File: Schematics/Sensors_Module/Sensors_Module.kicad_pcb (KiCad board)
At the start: 2 copper layers, 69.5 x 60 mm, 1 part, among them J6 Stack Male Edge Connector

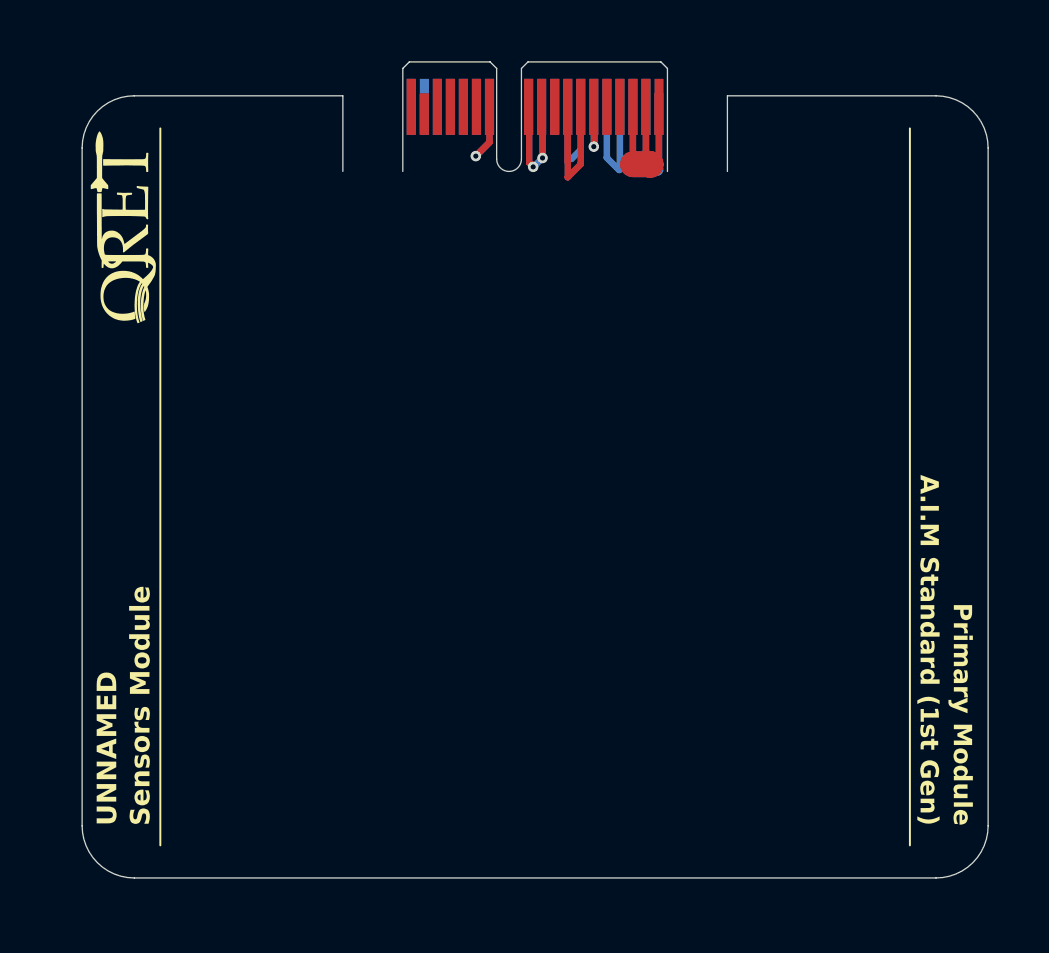
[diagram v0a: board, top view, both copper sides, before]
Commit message: Completed PCB layout
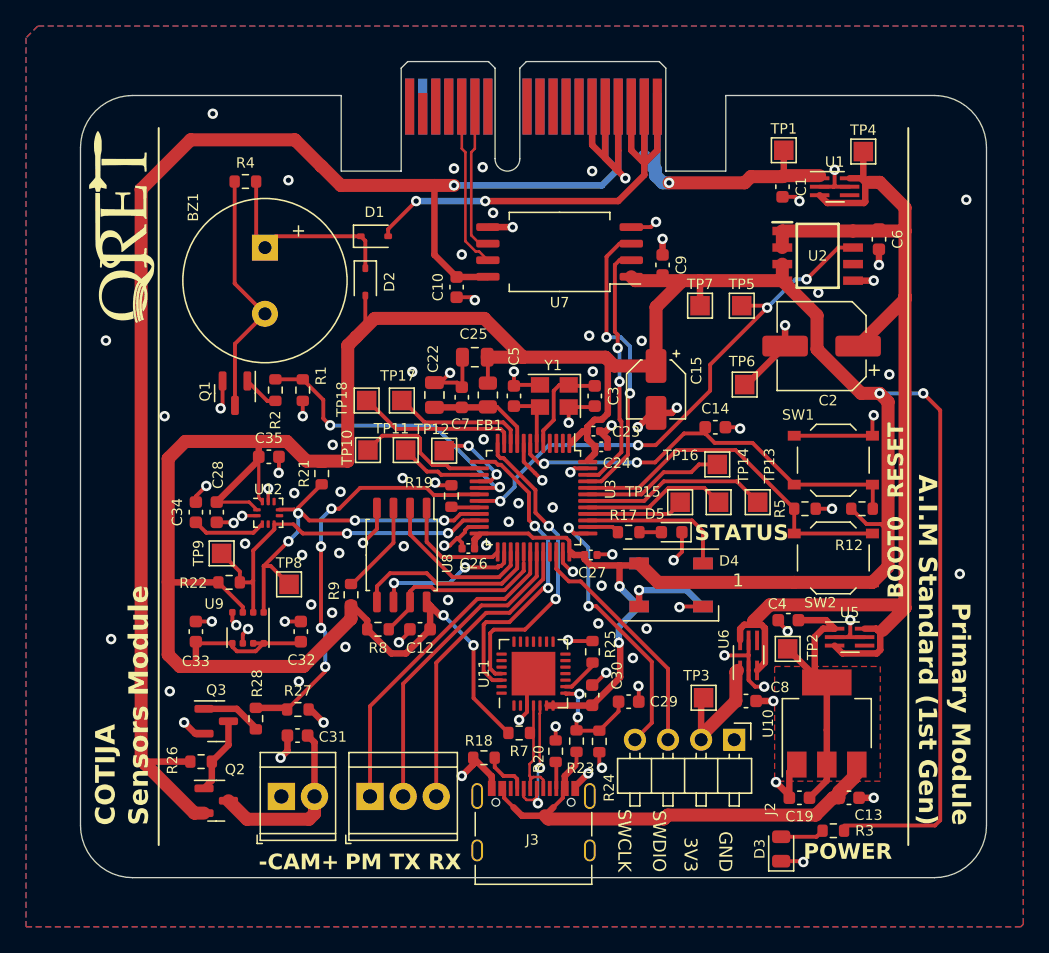
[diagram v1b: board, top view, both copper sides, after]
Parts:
- added BZ1: PKM13EPYH4000, footprints:Buzzer_12.6x9.5RM5.0, F.Cu at (101.1, 58.5)
- added C1: 1uF, Capacitor_SMD:C_0603_1608Metric, F.Cu at (140.8, 55.1)
- added C10: 0.1u, Capacitor_SMD:C_0603_1608Metric, F.Cu at (115.8, 62.8)
- added C12: 100nF, Capacitor_SMD:C_0603_1608Metric, F.Cu at (113.0, 89.0)
- added C13: 10uF, Capacitor_SMD:C_0603_1608Metric, F.Cu at (145.9, 102.0)
- added C14: 100nF, Capacitor_SMD:C_0603_1608Metric, F.Cu at (135.7, 73.5)
- added C15: 10uF, Capacitor_SMD:CP_Elec_4x5.4, F.Cu at (131.1, 70.7)
- added C19: 10uF, Capacitor_SMD:C_0603_1608Metric, F.Cu at (142.1, 102.0)
- added C2: 100uF, Capacitor_SMD:CP_Elec_6.3x5.9, F.Cu at (143.8, 67.3)
- added C22: 1uF, Capacitor_SMD:C_0805_2012Metric, F.Cu at (114.1, 71.1)
- added C23: 100n, Capacitor_SMD:C_0402_1005Metric, F.Cu at (126.3, 73.8)
- added C24: 100n, Capacitor_SMD:C_0402_1005Metric, F.Cu at (126.9, 75.0)
- added C25: 1uF, Capacitor_SMD:C_0805_2012Metric, F.Cu at (117.2, 68.2)
- added C26: 100n, Capacitor_SMD:C_0402_1005Metric, F.Cu at (116.7, 82.8)
- added C27: 100n, Capacitor_SMD:C_0402_1005Metric, F.Cu at (126.1, 83.3)
- added C28: 1uF, Capacitor_SMD:C_0603_1608Metric, F.Cu at (97.4, 80.1)
- added C29: 1uF, Capacitor_SMD:C_0603_1608Metric, F.Cu at (129.0, 94.6)
- added C3: 10p, Capacitor_SMD:C_0603_1608Metric, F.Cu at (126.4, 71.2)
- added C30: 10uF, Capacitor_SMD:C_0603_1608Metric, F.Cu at (126.2, 94.1)
- added C31: 10uF, Capacitor_SMD:C_0603_1608Metric, F.Cu at (103.6, 97.2)
- added C32: 100nF, Capacitor_SMD:C_0603_1608Metric, F.Cu at (103.8, 89.2)
- added C33: 100nF, Capacitor_SMD:C_0603_1608Metric, F.Cu at (95.8, 89.2)
- added C34: 1uF, Capacitor_SMD:C_0603_1608Metric, F.Cu at (95.8, 80.1)
- added C35: 1uF, Capacitor_SMD:C_0603_1608Metric, F.Cu at (101.4, 75.8)
- added C4: 1uF, Capacitor_SMD:C_0603_1608Metric, F.Cu at (141.2, 88.3)
- added C5: 10p, Capacitor_SMD:C_0603_1608Metric, F.Cu at (120.2, 71.2)
- added C6: 0.1uF, Capacitor_SMD:C_0603_1608Metric, F.Cu at (148.2, 59.1)
- added C7: 10n, Capacitor_SMD:C_0603_1608Metric, F.Cu at (116.2, 71.2)
- added C8: 1uF, Capacitor_SMD:C_0603_1608Metric, F.Cu at (138.0, 94.5)
- added C9: 0.1u, Capacitor_SMD:C_0603_1608Metric, F.Cu at (131.6, 61.1)
- added D1: 1N5819WS, Diode_SMD:D_SOD-323, F.Cu at (109.5, 58.9)
- added D2: 1N5819WS, Diode_SMD:D_SOD-323, F.Cu at (108.8, 62.4)
- added D3: PWR_LED (GRN), LED_SMD:LED_0805_2012Metric, F.Cu at (140.7, 105.9)
- added D4: WS2812B, LED_SMD:LED_WS2812B_PLCC4_5.0x5.0mm_P3.2mm, F.Cu at (132.2, 85.7)
- added D5: DB_LED (YLW), LED_SMD:LED_0603_1608Metric, F.Cu at (132.3, 81.6)
- added D6: WS2812B, LED_SMD:LED_WS2812B_PLCC4_5.0x5.0mm_P3.2mm, B.Cu at (132.2, 85.7)
- added FB1: 100R, Resistor_SMD:R_0805_2012Metric, F.Cu at (118.2, 71.1)
- added J1: Stack Male Edge Connector, Connector_PCBEdge:BUS_PCIexpress_x1, F.Cu at (131.2, 49.0)
- added J2: SWD_01x04_Pin, SWD_Header:SWD_PinHeader_1x04_P2.54mm_Horizontal, F.Cu at (137.1, 97.5)
- added J3: USB_C_Female_USB2_Small, footprints:USB_C_DB-108PWB, F.Cu at (121.7, 103.8)
- added J7: CAM_DAT, TerminalBlock_TE-Connectivity:TerminalBlock_TE_282834-3_1x03_P2.54mm_Horizontal, F.Cu at (109.2, 101.9)
- added Q1: AO3400A, Package_TO_SOT_SMD:SOT-23, F.Cu at (98.8, 70.9)
- added Q2: AO3401A, Package_TO_SOT_SMD:SOT-23, F.Cu at (97.4, 102.2)
- added Q3: AO3400A, Package_TO_SOT_SMD:SOT-23, F.Cu at (97.4, 96.1)
- added R1: 10k, Resistor_SMD:R_0603_1608Metric, F.Cu at (104.0, 70.7)
- added R12: 10k, Resistor_SMD:R_0603_1608Metric, F.Cu at (146.9, 79.8)
- added R17: 680R, Resistor_SMD:R_0603_1608Metric, F.Cu at (129.0, 81.6)
- added R18: 5.1k, Resistor_SMD:R_0603_1608Metric, F.Cu at (117.9, 98.9)
- added R19: 100k, Resistor_SMD:R_0603_1608Metric, F.Cu at (115.4, 78.8)
- added R2: 510R, Resistor_SMD:R_0603_1608Metric, F.Cu at (101.9, 70.7)
- added R20: 5.1k, Resistor_SMD:R_0603_1608Metric, F.Cu at (123.4, 98.4)
- added R21: 4.7k, Resistor_SMD:R_0603_1608Metric, F.Cu at (105.5, 77.1)
- added R22: 4.7k, Resistor_SMD:R_0603_1608Metric, F.Cu at (98.3, 85.5)
- added R23: 22k, Resistor_SMD:R_0603_1608Metric, F.Cu at (125.0, 97.6)
- added R24: 47k, Resistor_SMD:R_0603_1608Metric, F.Cu at (126.8, 97.7)
- added R25: 1k, Resistor_SMD:R_0603_1608Metric, F.Cu at (126.2, 90.8)
- added R26: 100k, Resistor_SMD:R_0603_1608Metric, F.Cu at (96.2, 99.2)
- added R27: 100k, Resistor_SMD:R_0603_1608Metric, F.Cu at (103.6, 95.2)
- added R28: 510, Resistor_SMD:R_0603_1608Metric, F.Cu at (100.4, 95.9)
- added R3: 3.3k, Resistor_SMD:R_0603_1608Metric, F.Cu at (144.7, 104.5)
- added R4: 1k, Resistor_SMD:R_0603_1608Metric, F.Cu at (99.6, 54.7)
- added R5: 100k, Resistor_SMD:R_0603_1608Metric, F.Cu at (142.5, 79.8)
- added R7: 1.5k, Resistor_SMD:R_0603_1608Metric, F.Cu at (120.6, 97.0)
- added R8: 10k, Resistor_SMD:R_0603_1608Metric, F.Cu at (109.8, 89.0)
- added R9: 10k, Resistor_SMD:R_0603_1608Metric, F.Cu at (107.7, 86.4)
- added SW1: SW_STM_RESET, Button_Switch_SMD:SW_Push_1P1T_XKB_TS-1187A, F.Cu at (144.7, 76.1)
- added SW2: SW_STM_BOOT_MODE, Button_Switch_SMD:SW_Push_1P1T_XKB_TS-1187A, F.Cu at (144.7, 83.6)
- added TP1: TP_VSTACK, TestPoint:TestPoint_Pad_1.5x1.5mm, F.Cu at (140.9, 52.3)
- added TP10: PA4, TestPoint:TestPoint_Pad_1.5x1.5mm, F.Cu at (109.0, 75.3)
- added TP11: PA5, TestPoint:TestPoint_Pad_1.5x1.5mm, F.Cu at (111.9, 75.3)
- added TP12: PA6, TestPoint:TestPoint_Pad_1.5x1.5mm, F.Cu at (114.8, 75.3)
- added TP13: PB6, TestPoint:TestPoint_Pad_1.5x1.5mm, F.Cu at (138.9, 79.3)
- added TP14: PB5, TestPoint:TestPoint_Pad_1.5x1.5mm, F.Cu at (135.9, 79.3)
- added TP15: PB4, TestPoint:TestPoint_Pad_1.5x1.5mm, F.Cu at (132.9, 79.3)
- added TP16: PB7, TestPoint:TestPoint_Pad_1.5x1.5mm, F.Cu at (135.8, 76.4)
- added TP17: PA0, TestPoint:TestPoint_Pad_1.5x1.5mm, F.Cu at (111.6, 71.5)
- added TP18: PA1, TestPoint:TestPoint_Pad_1.5x1.5mm, F.Cu at (108.9, 71.5)
- added TP2: TP_VUSB, TestPoint:TestPoint_Pad_1.5x1.5mm, F.Cu at (141.2, 90.5)
- added TP3: TP_VSWD, TestPoint:TestPoint_Pad_1.5x1.5mm, F.Cu at (134.8, 94.3)
- added TP4: TP_MUX, TestPoint:TestPoint_Pad_1.5x1.5mm, F.Cu at (147.0, 52.4)
- added TP5: TP_ISENSE, TestPoint:TestPoint_Pad_1.5x1.5mm, F.Cu at (137.7, 64.2)
- added TP6: TP_GND, TestPoint:TestPoint_Pad_1.5x1.5mm, F.Cu at (137.9, 70.3)
- added TP7: TP_3V3, TestPoint:TestPoint_Pad_1.5x1.5mm, F.Cu at (134.5, 64.2)
- added TP8: TP_SCL, TestPoint:TestPoint_Pad_1.5x1.5mm, F.Cu at (103.0, 85.6)
- added TP9: TP_SDA, TestPoint:TestPoint_Pad_1.5x1.5mm, F.Cu at (97.8, 83.2)
- added U1: LM66100DCKR, LMR66100:SC-70-6_Handsoldering, F.Cu at (144.8, 55.1)
- added U10: AMS1117-3.3, Package_TO_SOT_SMD:SOT-223-3_TabPin2, F.Cu at (144.2, 96.3)
- added U11: CP2102N-Axx-xQFN28, Package_DFN_QFN:QFN-28-1EP_5x5mm_P0.5mm_EP3.35x3.35mm, F.Cu at (121.7, 92.5)
- added U12: BM1422AGMV, Package_LGA:Rohm_MLGA010V020A_LGA-10_2x2mm_P0.45mm_LayoutBorder_3x2y, F.Cu at (101.3, 80.1)
- added U2: ACS70331EOLC, footprints:SOIC127P600X175-8N, F.Cu at (143.5, 60.4)
- added U3: STM32F103CBT6, Package_QFP:LQFP-48_7x7mm_P0.5mm, F.Cu at (121.7, 79.0)
- added U5: LM66100DCKR, LMR66100:SC-70-6_Handsoldering, F.Cu at (145.9, 89.7)
- added U6: LM66100DCKR, LMR66100:SC-70-6_Handsoldering, F.Cu at (138.2, 91.0)
- added U7: ISO1042BDWVR, ISO1042:SOIC-8 ISO1042BDWV, F.Cu at (123.7, 60.1)
- added U8: W25Q128JVS, Package_SO:SOIC-8_5.23x5.23mm_P1.27mm, F.Cu at (111.6, 83.3)
- added U9: BME680, Package_LGA:Bosch_LGA-8_3x3mm_P0.8mm_ClockwisePinNumbering, F.Cu at (99.8, 88.9)
- added Y1: X322516MMB4SI, Crystal:Crystal_SMD_3225-4Pin_3.2x2.5mm, F.Cu at (123.3, 71.2)
- J6: value Stack Male Edge Connector -> CAM_PWR; footprint Connector_PCBEdge:BUS_PCIexpress_x1 -> TerminalBlock_TE-Connectivity:TerminalBlock_TE_282834-2_1x02_P2.54mm_Horizontal
- moved J6 60.3 mm to (102.4, 101.9), turned to 0 degrees
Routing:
- net +3.3V: track 0.00 -> 304.0 mm, vias 0 -> 6
- net GND: track 0.00 -> 145.2 mm, vias 0 -> 100
- net +5V: track 0.00 -> 114.1 mm, vias 0 -> 1
- net V_MUX: track 0.00 -> 87.1 mm
- net (no net): track 78.1 -> 0.00 mm, vias 4 -> 0
- net CURR_SENSE: track 0.00 -> 40.3 mm, vias 0 -> 4
- net 5V_RAW: track 0.00 -> 39.9 mm
- net +BATT: track 0.00 -> 36.7 mm, vias 0 -> 2
- net STM_RESET: track 0.00 -> 32.3 mm, vias 0 -> 2
- net CAM_PWR: track 0.00 -> 31.8 mm, vias 0 -> 4
- net SCL: track 0.00 -> 30.1 mm, vias 0 -> 4
- net SDA: track 0.00 -> 27.8 mm, vias 0 -> 2
- net BOOT0: track 0.00 -> 26.8 mm
- net CAM_TX: track 0.00 -> 25.1 mm
- net V_PSU: track 0.00 -> 25.0 mm, vias 0 -> 1
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- added copper zone on B.Cu, net GND
- added copper zone on F.Cu, net GND
- added copper zone on F.Cu, net V_REGUSB
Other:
- outline, holes or cut-outs redrawn
- board text added: "-CAM+"
- board text added: "BOOT0"
- board text added: "COTIJA"
- board text added: "Cotija Rev 1.0 QRET May 2024 Ethan Toste Kennan Bays"
- board text added: "JLCJLCJLCJLC"
- board text added: "PM TX RX"
- board text added: "POWER"
- board text added: "RESET"
- board text added: "STATUS"
- board text removed: "UNNAMED"

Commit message: Final tweaks
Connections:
- net D+ renamed CAN_H
- net D- renamed CAN_L
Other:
- board text added: "."
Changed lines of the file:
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@@
       (plot_on_all_layers_selection 0x0000000_00000000)
       (disableapertmacros false)
-      (usegerberextensions false)
-      (usegerberattributes true)
-      (usegerberadvancedattributes true)
-      (creategerberjobfile true)
+      (usegerberextensions true)
+      (usegerberattributes false)
+      (usegerberadvancedattributes false)
+      (creategerberjobfile false)
       (dashed_line_dash_ratio 12.000000)
       (dashed_line_gap_ratio 3.000000)
@@
       (psa4output false)
       (plotreference true)
-      (plotvalue true)
+      (plotvalue false)
       (plotinvisibletext false)
       (sketchpadsonfab false)
-      (subtractmaskfromsilk false)
+      (subtractmaskfromsilk true)
       (outputformat 1)
       (mirror false)
-      (drillshape 1)
+      (drillshape 0)
       (scaleselection 1)
-      (outputdirectory "")
+      (outputdirectory "gerbers/")
     )
   )
@@
   (net 110 "unconnected-(U12-TEST2-Pad6)")
   (net 111 "unconnected-(U12-DRDY-Pad8)")
-  (net 112 "D+")
-  (net 113 "D-")
+  (net 112 "CAN_L")
+  (net 113 "CAN_H")
   (footprint "Resistor_SMD:R_0603_1608Metric" (layer "F.Cu")
     (at 104 70.7 90)
@@
       (net 4 "GND") (pinfunction "GND2") (pintype "power_in"))
     (pad "6" smd roundrect (at 5.5 0.635 180) (size 1.8 0.6) (layers "F.Cu" "F.Paste" "F.Mask") (roundrect_rratio 0.25)
-      (net 113 "D-") (pinfunction "CANL") (pintype "bidirectional"))
+      (net 112 "CAN_L") (pinfunction "CANL") (pintype "bidirectional"))
     (pad "7" smd roundrect (at 5.5 -0.635 180) (size 1.8 0.6) (layers "F.Cu" "F.Paste" "F.Mask") (roundrect_rratio 0.25)
-      (net 112 "D+") (pinfunction "CANH") (pintype "bidirectional"))
+      (net 113 "CAN_H") (pinfunction "CANH") (pintype "bidirectional"))
     (pad "8" smd roundrect (at 5.5 -1.905 180) (size 1.8 0.6) (layers "F.Cu" "F.Paste" "F.Mask") (roundrect_rratio 0.25)
       (net 12 "+5V") (pinfunction "VCC2") (pintype "power_in"))
@@
       (net 25 "unconnected-(J1-GND_B-PadA12)") (pinfunction "GND_B") (pintype "passive+no_connect"))
     (pad "B13" connect rect (at 14 0 180) (size 0.7 4.3) (layers "F.Cu" "F.Mask")
-      (net 113 "D-") (pinfunction "CAN_L") (pintype "bidirectional"))
+      (net 112 "CAN_L") (pinfunction "CAN_L") (pintype "bidirectional"))
     (pad "B14" connect rect (at 15 0 180) (size 0.7 4.3) (layers "F.Cu" "F.Mask")
-      (net 112 "D+") (pinfunction "CAN_H") (pintype "bidirectional"))
+      (net 113 "CAN_H") (pinfunction "CAN_H") (pintype "bidirectional"))
     (pad "B15" connect rect (at 16 0 180) (size 0.7 4.3) (layers "F.Cu" "F.Mask")
       (net 35 "unconnected-(J1-Reserved-PadB15)") (pinfunction "Reserved") (pintype "no_connect"))
@@
     (fp_line (start 1 0.625) (end -1 0.625)
       (stroke (width 0.1) (type solid)) (layer "F.Fab"))
-    (pad "1" smd roundrect (at -0.9125 0 90) (size 1.025 1.4) (layers "F.Cu" "F.Paste" "F.Mask") (roundrect_rratio 0.243902)
+    (pad "1" smd roundrect (at -0.9125 0 90) (size 1.025 1.4) (layers "F.Cu" "F.Paste" "F.Mask") (roundrect_rratio 0.243902439)
       (net 9 "+3.3VA") (pintype "passive"))
-    (pad "2" smd roundrect (at 0.9125 0 90) (size 1.025 1.4) (layers "F.Cu" "F.Paste" "F.Mask") (roundrect_rratio 0.243902)
+    (pad "2" smd roundrect (at 0.9125 0 90) (size 1.025 1.4) (layers "F.Cu" "F.Paste" "F.Mask") (roundrect_rratio 0.243902439)
       (net 11 "+3.3V") (pintype "passive"))
     (model "${KICAD6_3DMODEL_DIR}/Resistor_SMD.3dshapes/R_0805_2012Metric.wrl"
@@
     (effects (font (size 1.2 1.2) (thickness 0.2) bold) (justify left bottom))
   )
+  (gr_text "." (at 98.2 87) (layer "F.SilkS")
+    (effects (font (size 1.2 1.2) (thickness 0.24) bold) (justify left bottom))
+  )
   (gr_text "Primary Module" (at 153.65 104.099998 270) (layer "F.SilkS")
     (effects (font (size 1.4 1.4) (thickness 0.25) bold) (justify right bottom))
@@
   (segment (start 128.3 70.05) (end 128.3 67.610663) (width 0.3) (layer "B.Cu") (net 87))
   (segment (start 128.3 67.610663) (end 128.15962 67.470283) (width 0.3) (layer "B.Cu") (net 87))
-  (segment (start 117.263604 60.065) (end 116.475 59.276396) (width 0.2) (layer "F.Cu") (net 112))
-  (segment (start 117.53 60.065) (end 117.263604 60.065) (width 0.2) (layer "F.Cu") (net 112))
-  (segment (start 116.475 59.276396) (end 116.475 52.450001) (width 0.2) (layer "F.Cu") (net 112))
-  (segment (start 116.2 52.175001) (end 116.2 48.95) (width 0.2) (layer "F.Cu") (net 112))
-  (segment (start 118.2 60.735) (end 117.53 60.065) (width 0.2) (layer "F.Cu") (net 112))
-  (segment (start 116.475 52.450001) (end 116.2 52.175001) (width 0.2) (layer "F.Cu") (net 112))
-  (segment (start 118.2 59.465) (end 117.566397 59.465) (width 0.2) (layer "F.Cu") (net 113))
-  (segment (start 116.925 58.823603) (end 116.925 52.450001) (width 0.2) (layer "F.Cu") (net 113))
-  (segment (start 117.2 52.175001) (end 117.2 48.95) (width 0.2) (layer "F.Cu") (net 113))
-  (segment (start 117.566397 59.465) (end 116.925 58.823603) (width 0.2) (layer "F.Cu") (net 113))
-  (segment (start 116.925 52.450001) (end 117.2 52.175001) (width 0.2) (layer "F.Cu") (net 113))
+  (segment (start 118.2 59.465) (end 117.566397 59.465) (width 0.2) (layer "F.Cu") (net 112))
+  (segment (start 116.925 58.823603) (end 116.925 52.450001) (width 0.2) (layer "F.Cu") (net 112))
+  (segment (start 117.2 52.175001) (end 117.2 48.95) (width 0.2) (layer "F.Cu") (net 112))
+  (segment (start 117.566397 59.465) (end 116.925 58.823603) (width 0.2) (layer "F.Cu") (net 112))
+  (segment (start 116.925 52.450001) (end 117.2 52.175001) (width 0.2) (layer "F.Cu") (net 112))
+  (segment (start 117.263604 60.065) (end 116.475 59.276396) (width 0.2) (layer "F.Cu") (net 113))
+  (segment (start 117.53 60.065) (end 117.263604 60.065) (width 0.2) (layer "F.Cu") (net 113))
+  (segment (start 116.475 59.276396) (end 116.475 52.450001) (width 0.2) (layer "F.Cu") (net 113))
+  (segment (start 116.2 52.175001) (end 116.2 48.95) (width 0.2) (layer "F.Cu") (net 113))
+  (segment (start 118.2 60.735) (end 117.53 60.065) (width 0.2) (layer "F.Cu") (net 113))
+  (segment (start 116.475 52.450001) (end 116.2 52.175001) (width 0.2) (layer "F.Cu") (net 113))
   (zone locked (net 7) (net_name "V_REGUSB") (layer "F.Cu") (name "Keepout") (hatch edge 0.5)
     (priority 1)

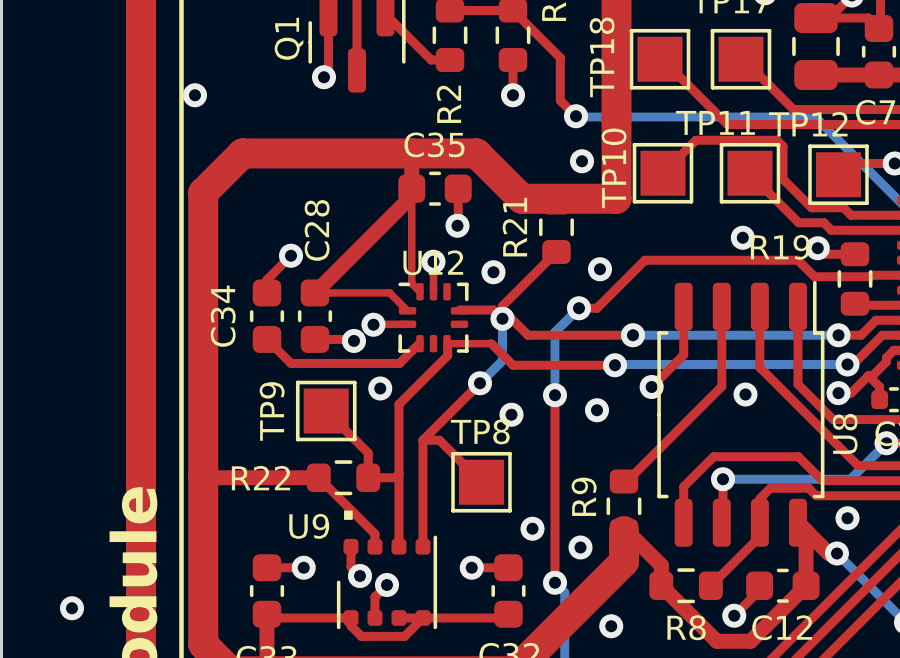
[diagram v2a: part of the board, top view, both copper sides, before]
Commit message: Fixed incorrect pinout for BM1422AGMV (Rev 1.0A)
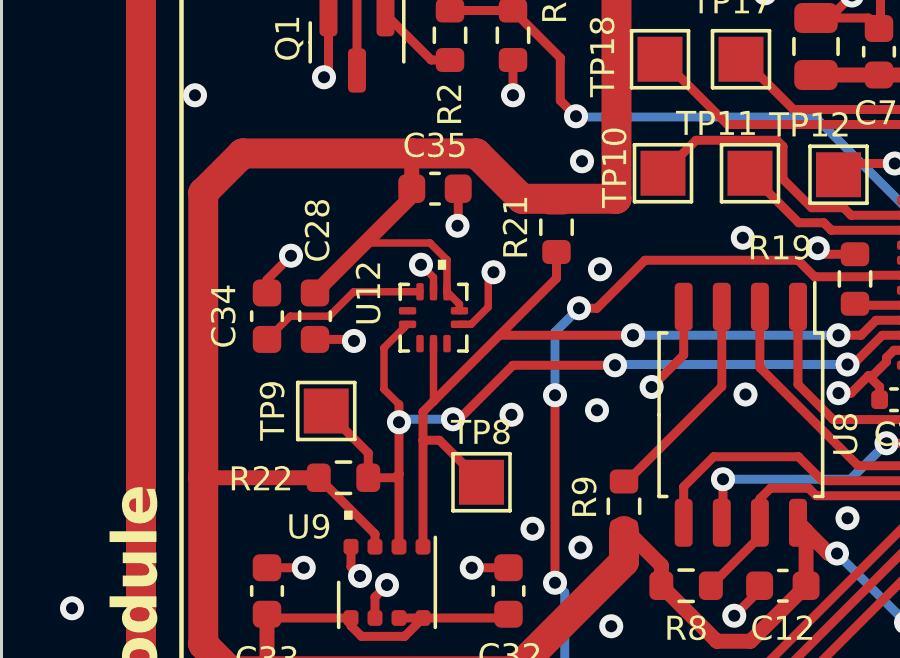
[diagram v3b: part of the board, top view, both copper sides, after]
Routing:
- net SDA: track 27.8 -> 30.4 mm, vias 2 -> 4
- net GND: track 145.2 -> 146.6 mm, vias 100 -> 98
- net SCL: track 30.1 -> 30.3 mm, vias 4 -> 2
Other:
- board text added: "Cotija Rev 1.0A QRET May 2024 Ethan Toste Kennan Bays"
- board text removed: "Cotija Rev 1.0 QRET May 2024 Ethan Toste Kennan Bays"

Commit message: Version bump to V2.0
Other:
- board text added: "COTIJA V2.0"
- board text added: "Cotija Rev 2.0 QRET Mar 2025 Ethan Toste Kennan Bays"
- board text removed: "COTIJA"
- board text removed: "Cotija Rev 1.0A QRET May 2024 Ethan Toste Kennan Bays"
- board text removed: "JLCJLCJLCJLC"
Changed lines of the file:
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@@
   (gr_line (start 106.95 53.9) (end 111.55 53.9)
     (stroke (width 0.1) (type default)) (layer "Edge.Cuts"))
-  (gr_text "Cotija Rev 1.0A\nQRET May 2024\n\nEthan Toste\nKennan Bays" (at 121.699999 57.3) (layer "B.SilkS")
+  (gr_text "Cotija Rev 2.0\nQRET Mar 2025\n\nEthan Toste\nKennan Bays" (at 121.699999 57.3) (layer "B.SilkS")
     (effects (font (size 1.5 1.5) (thickness 0.25)) (justify top mirror))
-  )
-  (gr_text "JLCJLCJLCJLC" (at 152.775 57.675 -90) (layer "B.SilkS")
-    (effects (font (size 1 1) (thickness 0.2) bold) (justify right bottom mirror))
   )
   (gr_text "Sensors Module" (at 92.3 104.099998 90) (layer "F.SilkS" knockout)
     (effects (font (size 1.5 1.5) (thickness 0.3) bold) (justify left bottom))
   )
-  (gr_text "COTIJA" (at 89.75 104.099998 90) (layer "F.SilkS" knockout)
+  (gr_text "COTIJA V2.0" (at 89.75 104.099998 90) (layer "F.SilkS" knockout)
     (effects (font (size 1.5 1.5) (thickness 0.3) bold) (justify left bottom))
   )
